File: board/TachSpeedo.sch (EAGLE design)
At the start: 13 parts, among them J1 1-770969-0, P1 M-1X04-SIP-100-32, P2 M-1X03-SIP-100-32, U1 D24V5FX, U2 LPC810M, U3 MC33152, U4 MAX3483

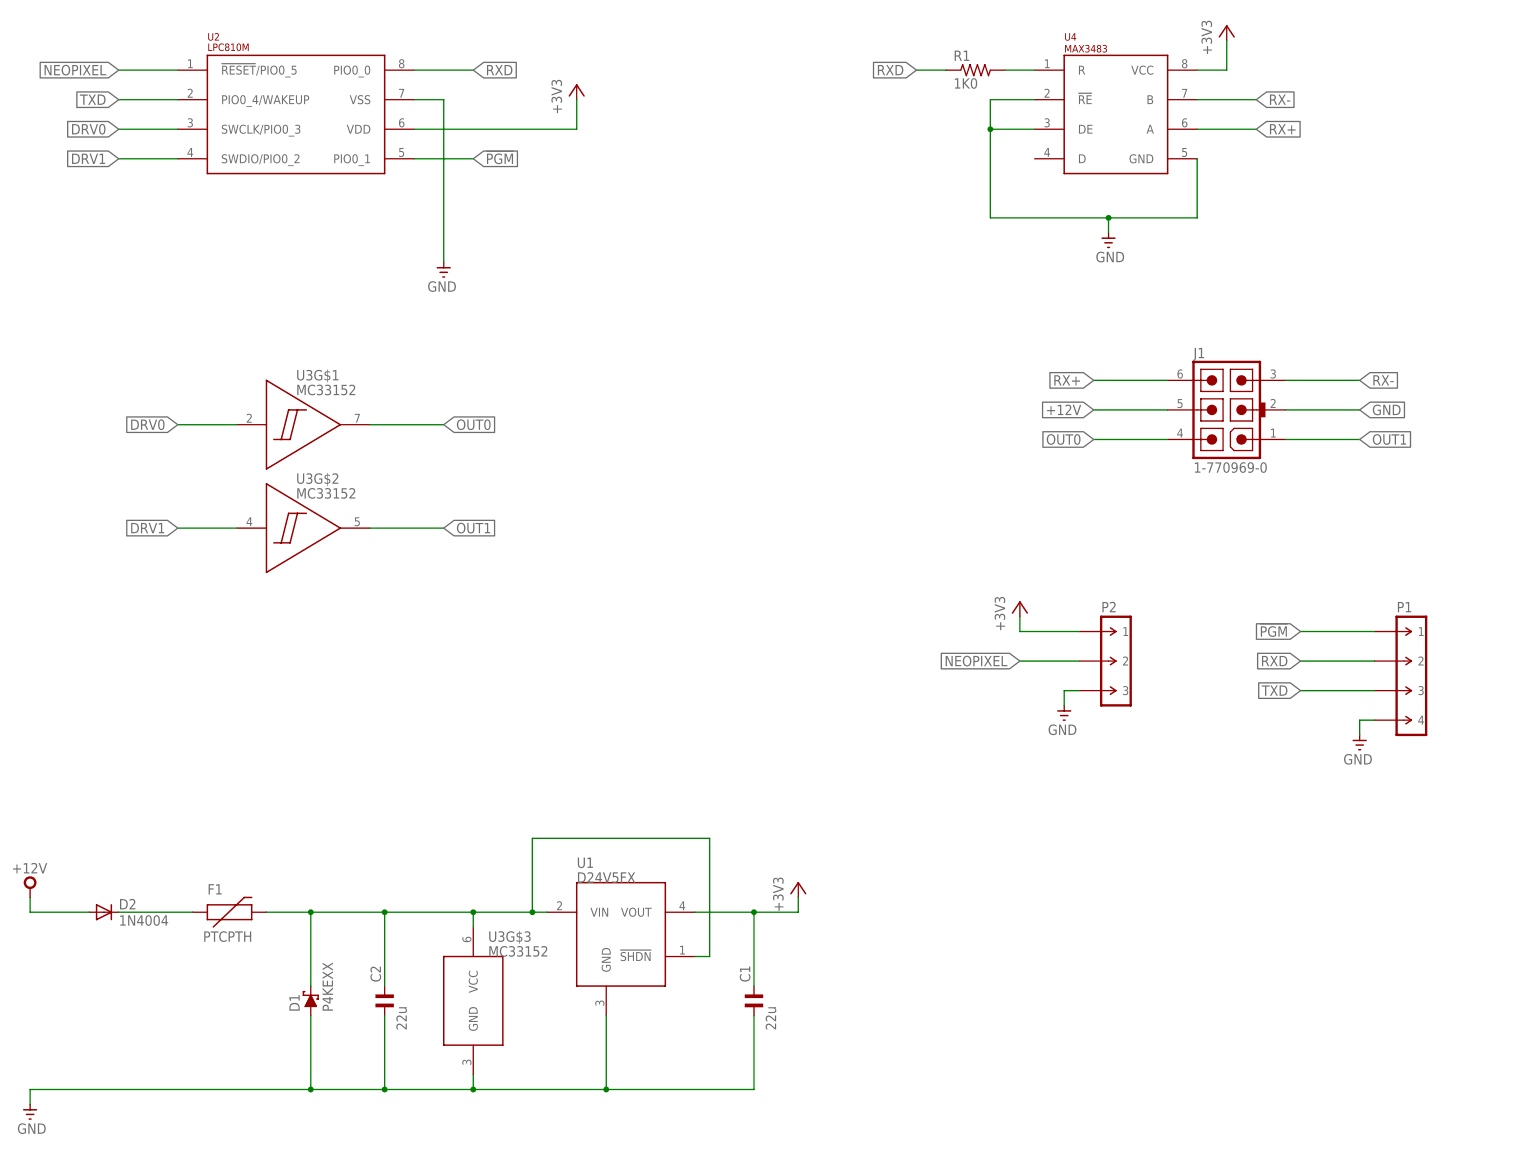
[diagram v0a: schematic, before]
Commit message: Update in anticipation of the r3 board.
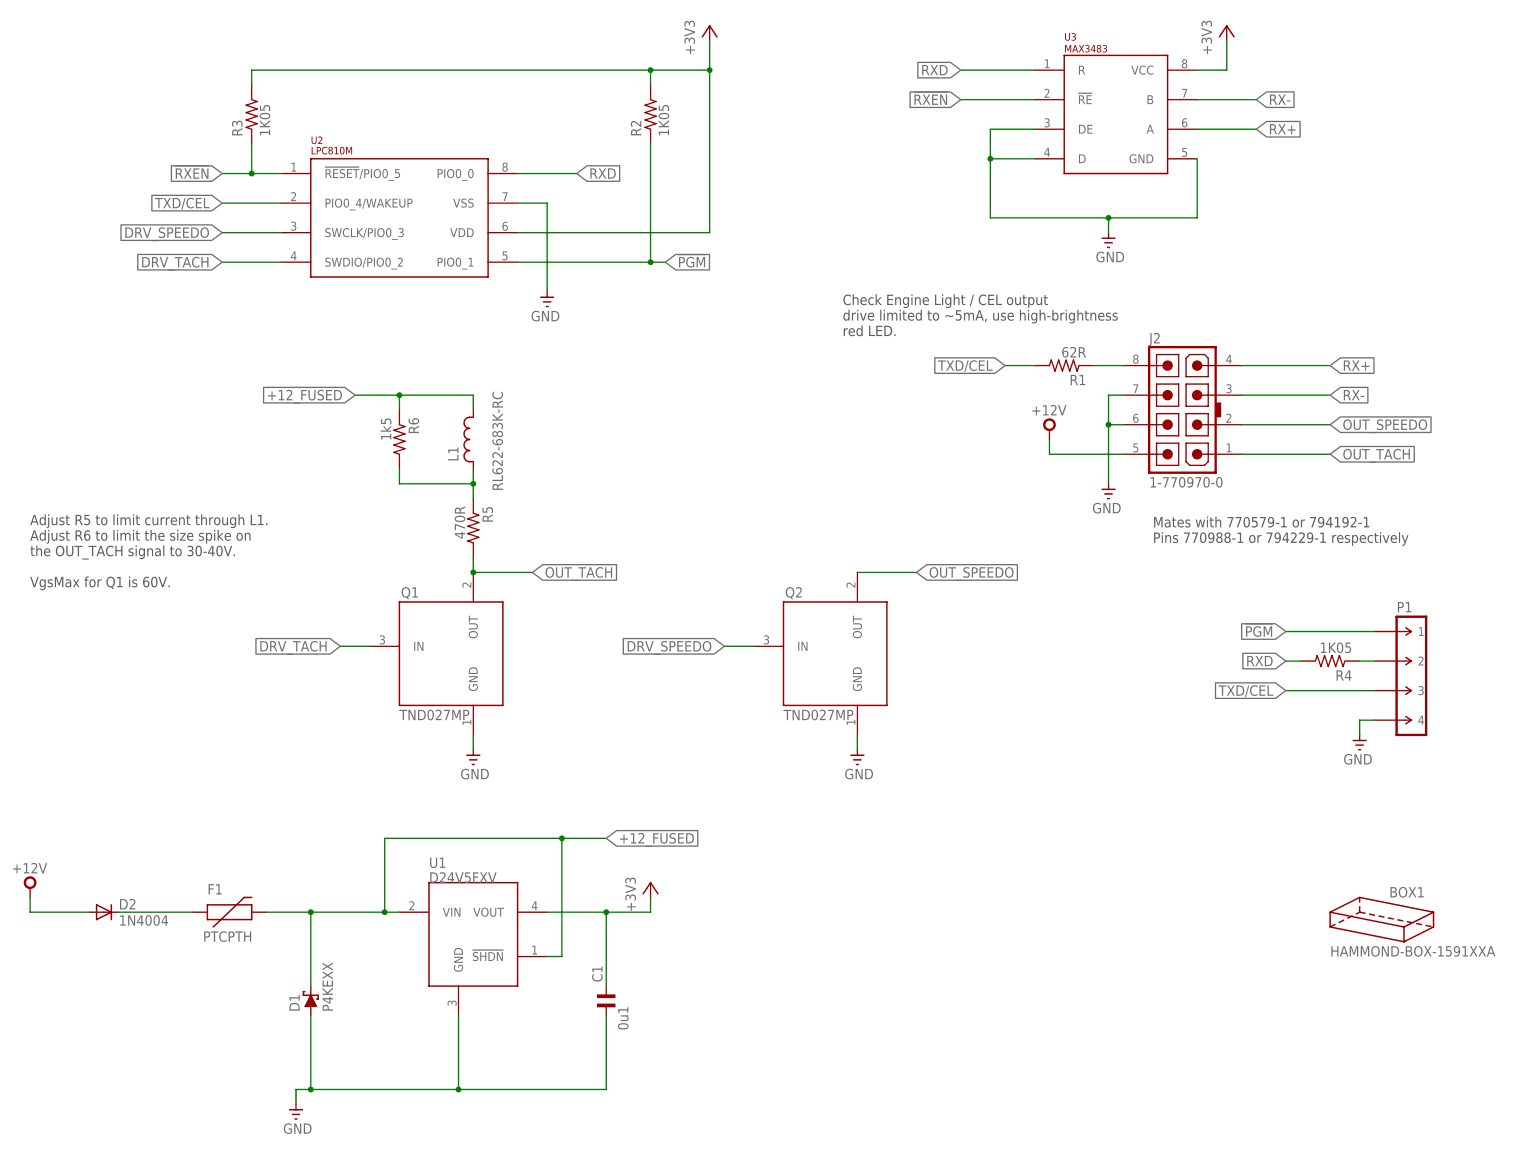
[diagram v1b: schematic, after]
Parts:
- removed C2: 22u, custom:C-EU050-024X044
- removed J1: 1-770969-0, custom:1-770969-0
- removed P2: M-1X03-SIP-100-32, custom:M-1X03-SIP-100-32
- removed U4: MAX3483, custom:MAX3483
- added BOX1: HAMMOND-BOX-1591XXA, custom:HAMMOND-BOX-1591XXA
- added J2: 1-770970-0, custom:1-770970-0
- added L1: RL622-683K-RC, custom:RL622
- added Q1, Q2: TND027MP, custom:TND027MP
- added R2, R3, R4: 1K05, custom:R-EU_0207/10
- added R5: 470R, custom:R-EU_0207/10
- added R6: 1k5, custom:R-EU_0207/10
- C1: value 22u -> 0u1; device custom:C-EU050-024X044 -> custom:C-EU025-024X044; PARTNO FK22X5R1E226M -> FK18X7R1E104K
- D2: PARTNO 1N4004-T -> 1N4004
- P1: value M-1X04-SIP-100-32 -> M-1X04-SIP-100-40; device custom:M-1X04-SIP-100-32 -> custom:M-1X04-SIP-100-40
- R1: value 1K0 -> 62R; PARTNO MFR-25FRF52-1K -> MFR-25FTE52-62R
- U1: value D24V5FX -> D24V5FXV; device custom:D24V5FX -> custom:D24V5FXV
- U3: value MC33152 -> MAX3483; device custom:MC33152 -> custom:MAX3483; PARTNO MC33152PG -> MAX3483CPA+
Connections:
- removed net DRV0: U2.SWCLK/PIO0_3, U3G$1.IN
- removed net DRV1: U2.SWDIO/PIO0_2, U3G$2.IN
- removed net N$1: C2.1, D1.C, F1.2, U1.!SHDN, U1.VIN, U3G$3.VCC
- removed net NEOPIXEL: P2.2, U2.!RESET!/PIO0_5
- removed net OUT0: J1.4, U3G$1.OUT
- removed net OUT1: J1.1, U3G$2.OUT
- removed net TXD: P1.3, U2.PIO0_4/WAKEUP
- new net !RXEN: R3.1, U2.!RESET!/PIO0_5, U3.!RE
- new net +12_FUSED: D1.C, F1.2, L1.2, R6.1, U1.!SHDN, U1.VIN
- new net DRV_SPEEDO: Q2.IN, U2.SWCLK/PIO0_3
- new net DRV_TACH: Q1.IN, U2.SWDIO/PIO0_2
- new net N$4: J2.8, R1.1
- new net N$6: L1.1, R5.1, R6.2
- new net OUT_SPEEDO: J2.2, Q2.OUT
- new net OUT_TACH: J2.1, Q1.OUT, R5.2
- new net TXD/CEL: P1.3, R1.2, U2.PIO0_4/WAKEUP
- net !PGM: now also R2.1
- net +12V: now also J2.5; no longer J1.5
- net +3V3: now also R2.2, R3.2, U3.VCC; no longer P2.1, U4.VCC
- net GND: now also J2.6, J2.7, Q1.GND, Q2.GND, U3.D, U3.DE, U3.GND; no longer C2.2, J1.2, P2.3, U3G$3.GND, U4.!RE, U4.DE, U4.GND
- net N$3: now also P1.2, R4.1; no longer R1.2, U4.R
- net RX+: now also J2.4, U3.A; no longer J1.6, U4.A
- net RX-: now also J2.3, U3.B; no longer J1.3, U4.B
- net RXD: now also R4.2, U3.R; no longer P1.2, R1.1
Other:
- note added: "Adjust R5 to limit current through L1. Adjust R6 to limit the size spike on the OUT_TACH signal to 30-40V. VgsMax for Q1 is 60V."
- note added: "Check Engine Light / CEL output drive limited to ~5mA, use high-brightness red LED."
- note added: "Mates with 770579-1 or 794192-1 Pins 770988-1 or 794229-1 respectively"
- moved on the sheet: C1, R1, U1, U2
